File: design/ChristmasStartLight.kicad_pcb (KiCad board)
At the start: 2 copper layers, 11 parts, among them P1 CONN_2, Q1 MPS2222A, SW1 MHSS1104, U1 TCL555CP

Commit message: ChristmasStarLight_v3
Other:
- board outline added: 21.7 x 83.8 mm
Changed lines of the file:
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@@
     (area 123.170245 51.59375 145.553501 136.980444)
     (thickness 1.6)
-    (drawings 6)
+    (drawings 10)
     (tracks 90)
     (zones 0)
@@
     (visible_elements 7FFFFF7F)
     (pcbplotparams
-      (layerselection 3178497)
+      (layerselection 284196865)
       (usegerberextensions true)
       (excludeedgelayer true)
@@
     )
   )
+  (gr_line (start 123.571 136.5377) (end 123.571 52.6923) (angle 90) (layer Edge.Cuts) (width 0.1))
+  (gr_line (start 145.2372 136.5377) (end 123.571 136.5377) (angle 90) (layer Edge.Cuts) (width 0.1))
+  (gr_line (start 132.0292 52.6923) (end 145.2372 136.5377) (angle 90) (layer Edge.Cuts) (width 0.1))
+  (gr_line (start 123.571 52.6923) (end 132.0292 52.6923) (angle 90) (layer Edge.Cuts) (width 0.1))
   (gr_text v1 (at 138.5316 108.2421 90) (layer F.SilkS)
     (effects (font (size 0.992 0.992) (thickness 0.1972)))

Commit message: some update
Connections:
- SW1 pad 2: N-000008 -> GND
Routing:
- net N-000008: track 3.27 -> 0.00 mm
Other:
- board text added: "+"
- board text added: "-"
- board text added: "v2"

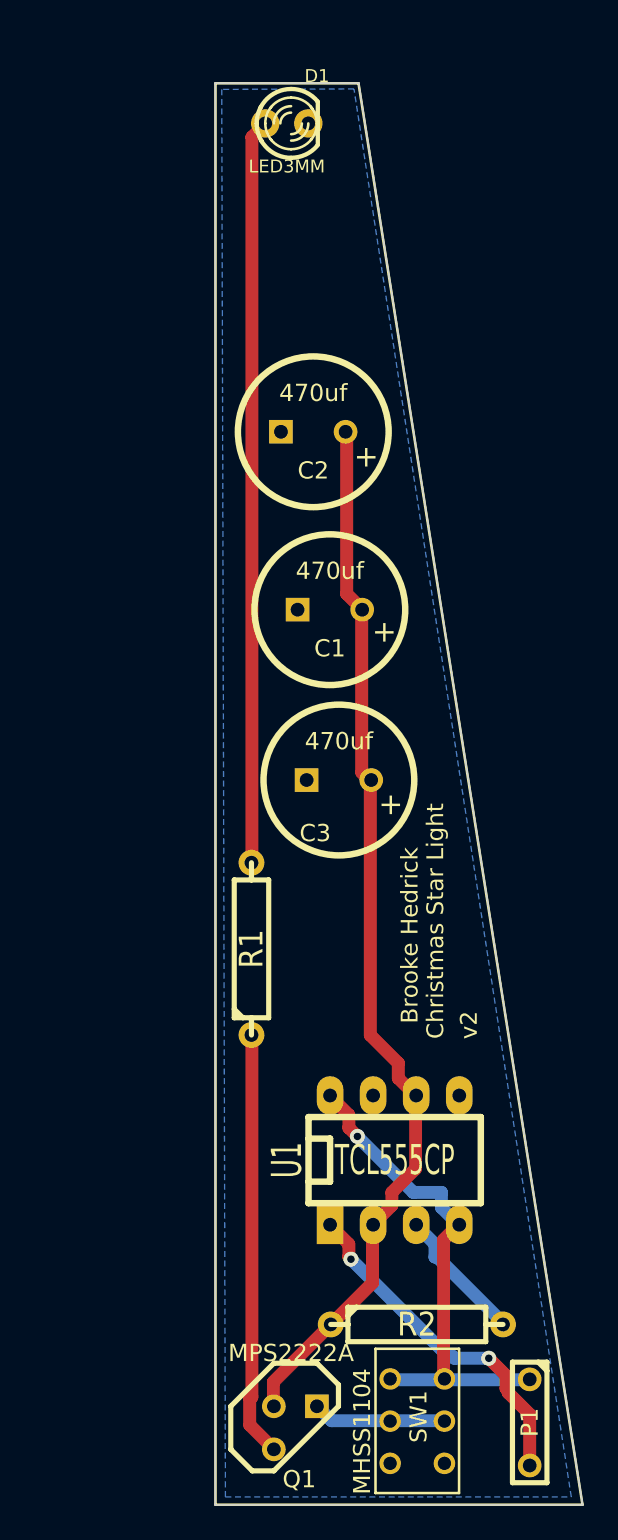
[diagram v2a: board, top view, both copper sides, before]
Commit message: first smd version v2
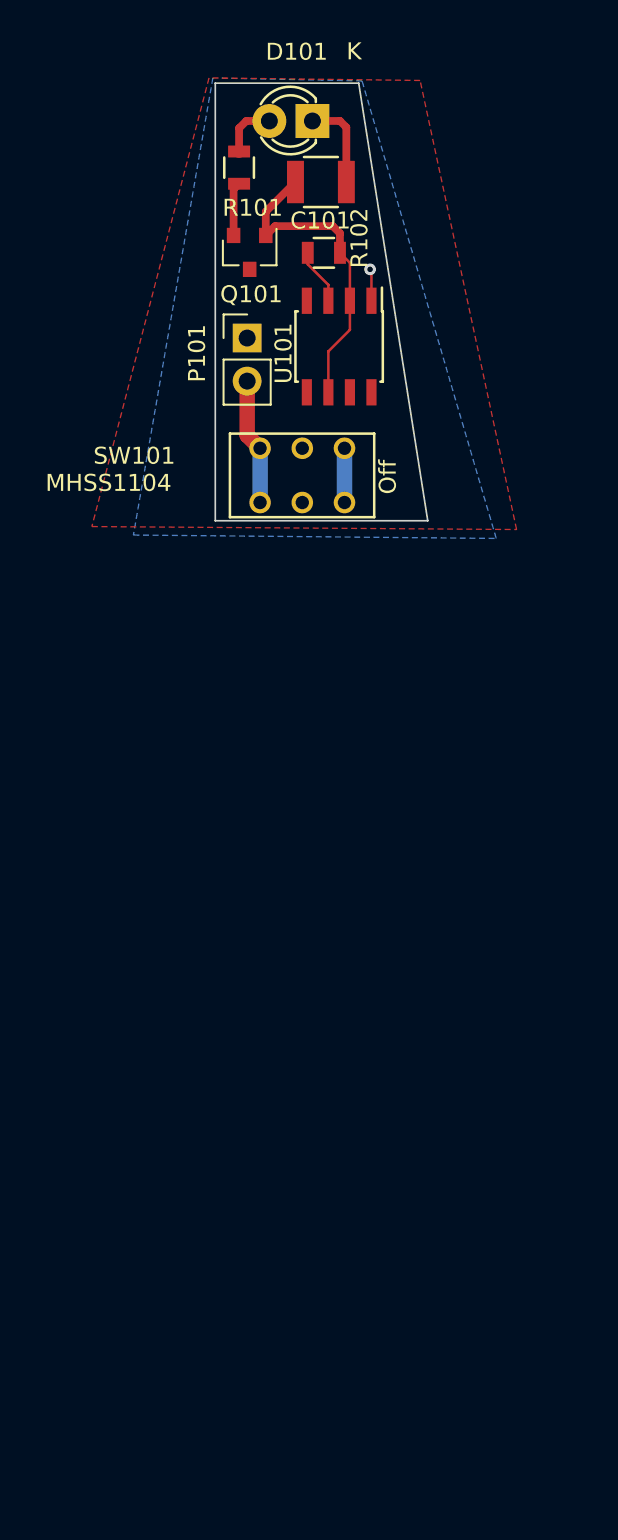
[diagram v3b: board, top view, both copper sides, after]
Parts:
- removed ?: VAL**, ChristmasStarBoardEdge
- removed C1, C2, C3: 470uf, C1.5V8V
- removed D1: LED3MM, LED-3MM
- removed P1: CONN_2, C2
- removed Q1: MPS2222A, TO92
- removed R1: 220, R4
- removed R2: 5.1K, R4
- removed SW1: MHSS1104, MHSS1104_MICROSWITCH_SPDT
- removed U1: TCL555CP, DIP-8__300_ELL
- added C101: C, Capacitors_SMD:C_1210, F.Cu at (129.8, 58.5)
- added D101: LED3MM, LEDs:LED-3MM, F.Cu at (129.3, 54.9)
- added P101: CONN_01X02, Pin_Headers:Pin_Header_Straight_1x02_Pitch2.54mm, F.Cu at (125.5, 67.7)
- added Q101: MMBT3904-7-F, bth-ic-footprint:SOT-23-3, F.Cu at (125.6, 62.7)
- added R101: 220, Resistors_SMD:R_0805, F.Cu at (125.0, 57.7)
- added R102: 300K, Resistors_SMD:R_0805, F.Cu at (130.0, 62.7)
- added SW101: MHSS1104, bth-switch:MHSS1104_MICROSWITCH_SPDT, F.Cu at (128.6, 75.8)
- added U101: ICM7555CBAZ-T, bth-ic-footprint:SOIC-8_3.9x4.9mm_Pitch1.27mm, F.Cu at (130.9, 68.2)
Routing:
- net N-0000010: track 63.2 -> 0.00 mm
- net N-000001: track 44.0 -> 0.00 mm
- net VCC: track 29.9 -> 0.00 mm, vias 1 -> 0
- net N-000004: track 25.1 -> 0.00 mm
- net Net-(C101-Pad1): track 0.00 -> 19.4 mm
- net GND: track 20.5 -> 7.26 mm, vias 2 -> 1
- net N-000003: track 8.17 -> 0.00 mm
- net N-000005: track 8.04 -> 0.00 mm
- net +9V: track 0.00 -> 7.48 mm
- net Net-(D101-Pad2): track 0.00 -> 3.35 mm
- net Net-(R102-Pad2): track 0.00 -> 3.33 mm
- net Net-(SW101-Pad2): track 0.00 -> 3.20 mm
- net Net-(Q101-Pad2): track 0.00 -> 3.18 mm
- added copper zone on F.Cu, net /VCC
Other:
- board size 21.7 x 83.8 mm -> 12.5 x 25.8 mm
- net class Default: clearance 0.254 -> 0.1524; trace_width 0.762 -> 0.1524; via_dia 0.889 -> 0.6858; via_drill 0.635 -> 0.3302
- net class Power added: clearance 0.1524, trace_width 0.6096, via_dia 0.6858, via_drill 0.3302
- rule trace_clearance: 0.254 -> 0.1524
- rule trace_min: 0.254 -> 0.1524
- rule via_min_drill: 0.508 -> 0.3302
- rule via_min_size: 0.889 -> 0.6858
- board text added: "1.9.2017"
- board text added: "Off"
- board text removed: "v1"

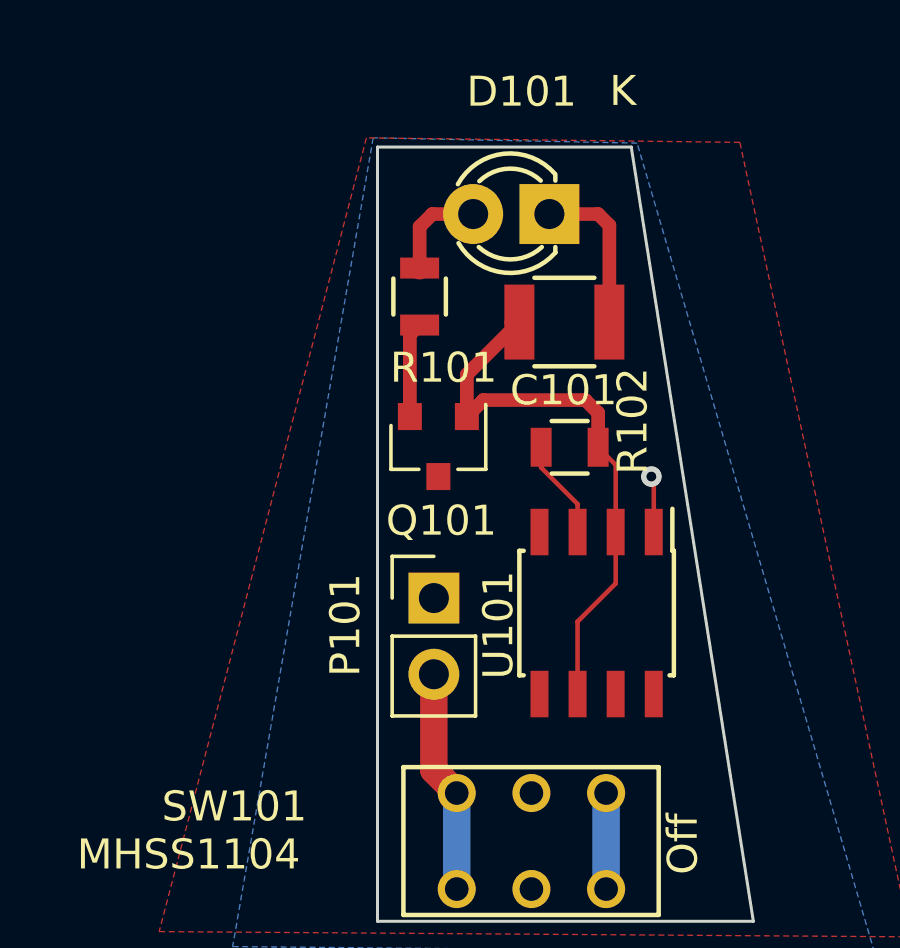
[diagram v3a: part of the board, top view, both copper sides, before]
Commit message: Started on v3 of the schematic.  Still need to do PCB layout.
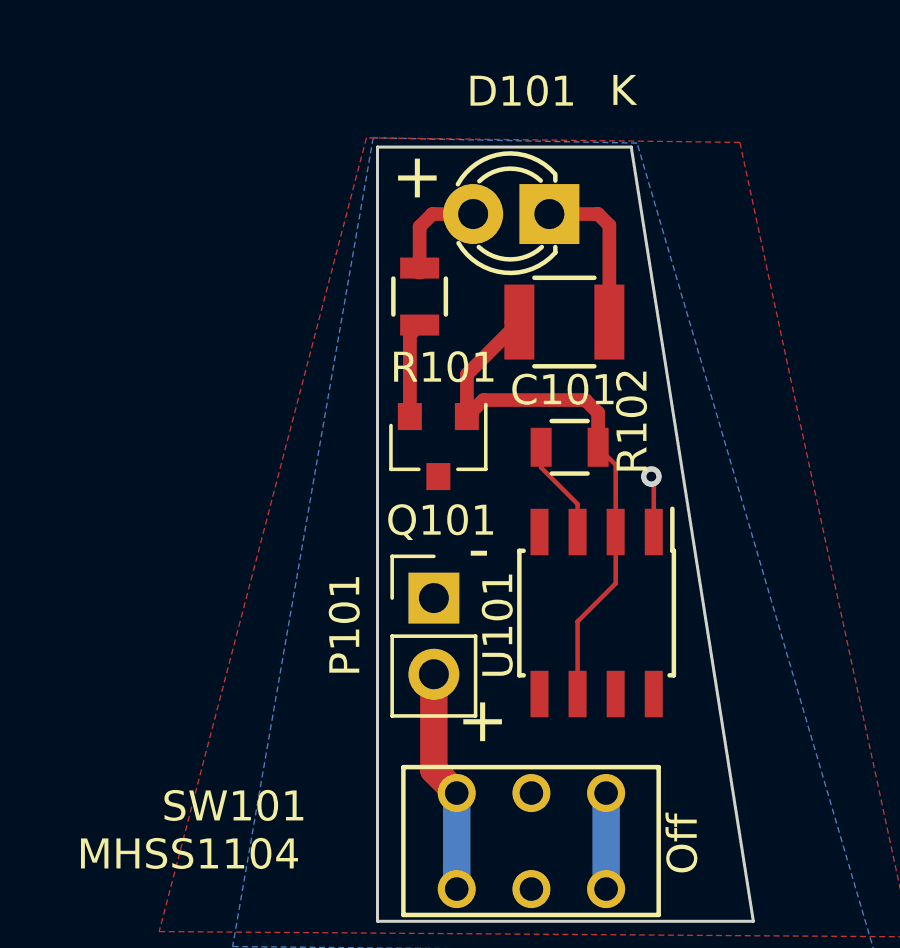
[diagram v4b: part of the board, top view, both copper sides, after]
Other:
- board text added: "v3"
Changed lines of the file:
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@@
     (links 17)
     (no_connects 0)
-    (area 123.520999 52.642299 136.150001 78.550001)
+    (area 113.170219 49.9226 271.710714 194.375)
     (thickness 1.6)
     (drawings 13)
@@
   )
   (setup
-    (last_trace_width 0.4572)
+    (last_trace_width 0.1524)
     (user_trace_width 0.1524)
     (user_trace_width 0.4572)
@@
     (effects (font (size 1 1) (thickness 0.125)))
   )
-  (gr_text + (at 124.9 53.675) (layer Dwgs.User)
+  (gr_text + (at 124.9 53.675) (layer F.SilkS)
     (effects (font (size 1.5 1.5) (thickness 0.3)))
   )
-  (gr_text - (at 126.95 66.1) (layer Dwgs.User)
+  (gr_text - (at 126.95 66.1) (layer F.SilkS)
     (effects (font (size 1.5 1.5) (thickness 0.3)))
   )
-  (gr_text + (at 127.075 71.8) (layer Dwgs.User)
+  (gr_text + (at 127.075 71.8) (layer F.SilkS)
     (effects (font (size 1.5 1.5) (thickness 0.3)))
   )
@@
   (gr_line (start 132.0292 52.6923) (end 136.1 78.5) (angle 90) (layer Edge.Cuts) (width 0.1))
   (gr_line (start 123.571 52.6923) (end 132.0292 52.6923) (angle 90) (layer Edge.Cuts) (width 0.1))
-  (gr_text v2 (at 131.6074 71.2072 90) (layer B.SilkS)
+  (gr_text v3 (at 131.6074 71.2072 90) (layer B.SilkS)
     (effects (font (size 0.992 0.992) (thickness 0.1972)) (justify mirror))
   )
